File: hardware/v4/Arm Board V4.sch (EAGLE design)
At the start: 49 parts, among them IC2 REG1118, U1 SN74LS241DW, U2 XBEE-1B3, U3 LSM9DS0

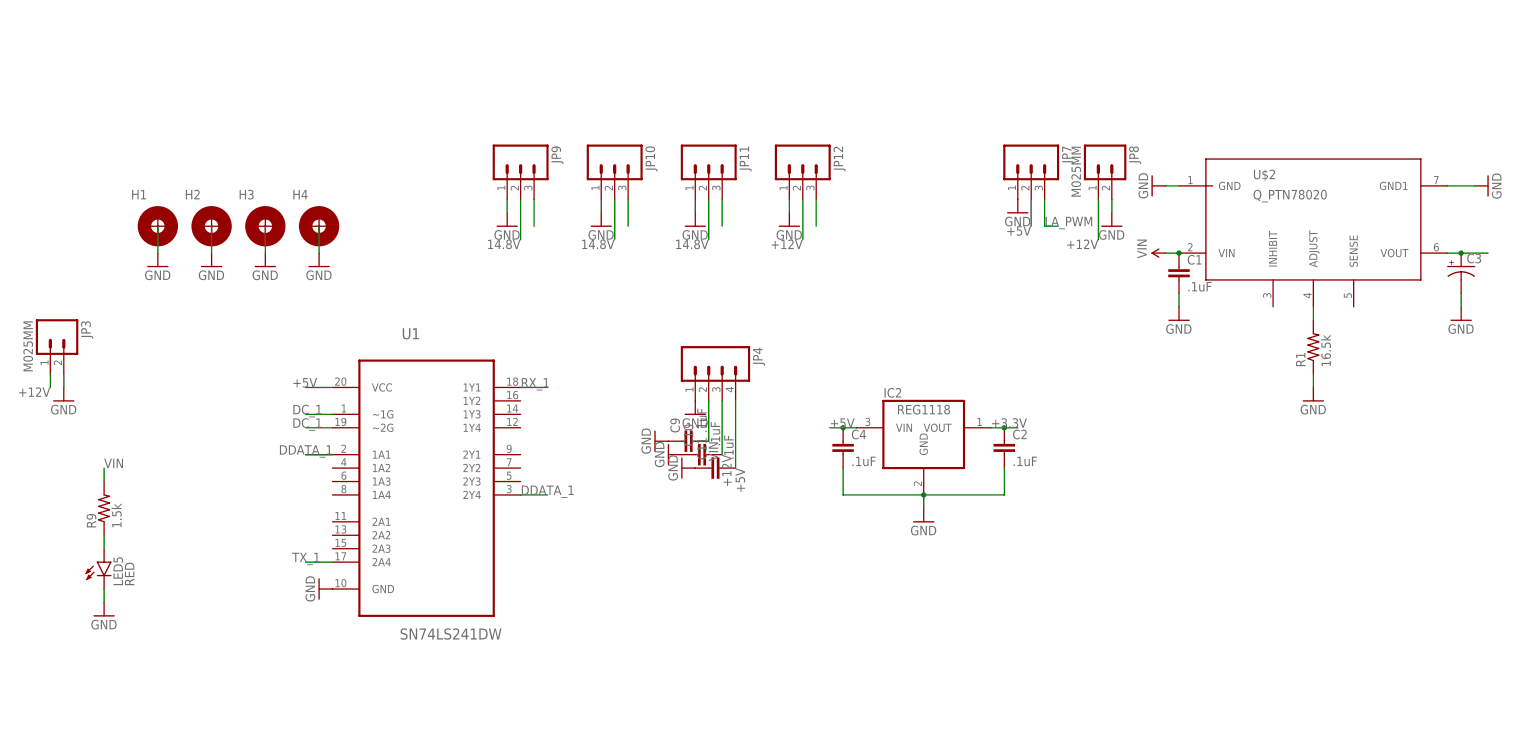
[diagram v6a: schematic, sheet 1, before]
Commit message: Just a few things with rearranging components
Moved some power connectors and a few pours
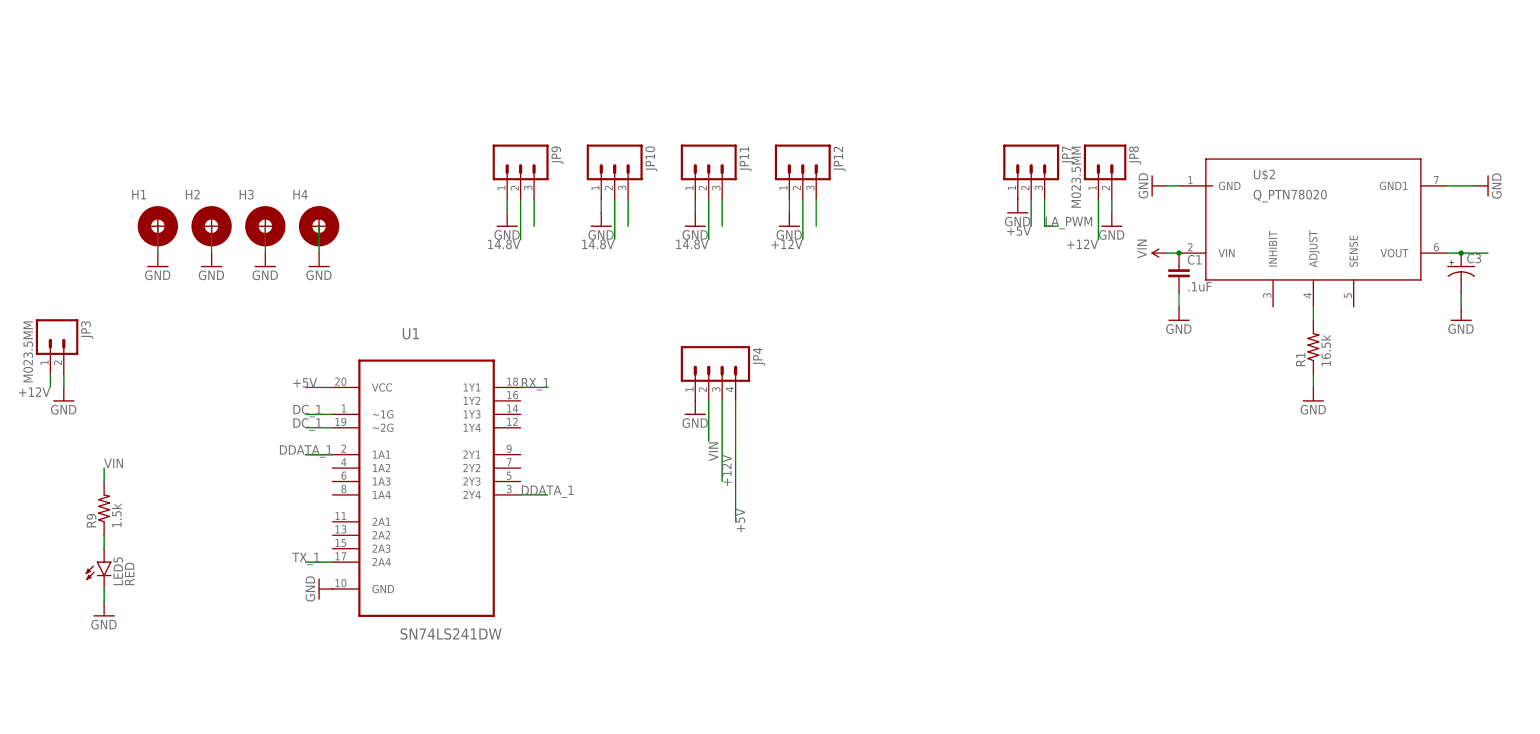
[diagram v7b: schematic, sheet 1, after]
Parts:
- removed C10, C11, C2, C4, C9: .1uF, SparkFun-Capacitors:CAP1206
- removed IC2: REG1118, burr-brown:REG1118
- JP3, JP8: value M025MM -> M023.5MM; device SparkFun-Connectors:M025MM -> SparkFun-Connectors:M023.5MM
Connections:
- removed net +3.3V: C2.1, IC2.VOUT, R12.2, R13.1, R14.1, U2.VDD
- net +12V: no longer C10.2
- net +3V3: now also R12.2, R13.1, R14.1, U2.VDD
- net +5V: no longer C11.2, C4.1, IC2.VIN
- net GND: no longer C10.1, C11.1, C2.2, C4.2, C9.1, IC2.GND
- net VIN: no longer C9.2
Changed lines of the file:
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@@
 <?xml version="1.0" encoding="utf-8"?>
 <!DOCTYPE eagle SYSTEM "eagle.dtd">
-<eagle version="6.5.0">
+<eagle version="7.1.0">
 <drawing>
 <settings>
@@
 <part name="U2" library="SparkFun" deviceset="XBEE-1" device="B3"/>
 <part name="JP7" library="SparkFun-Connectors" deviceset="M03" device="POLAR"/>
-<part name="JP8" library="SparkFun-Connectors" deviceset="M02" device="5MM"/>
+<part name="JP8" library="SparkFun-Connectors" deviceset="M02" device="3.5MM" value="M023.5MM"/>
 <part name="JP9" library="SparkFun-Connectors" deviceset="M03" device="POLAR"/>
 <part name="JP10" library="SparkFun-Connectors" deviceset="M03" device="POLAR"/>
@@
 <part name="C3" library="SparkFun-Passives" deviceset="CAP_POL" device="C"/>
 <part name="U$4" library="MAX3077" deviceset="MAX3077" device=""/>
-<part name="JP3" library="SparkFun-Connectors" deviceset="M02" device="5MM"/>
+<part name="JP3" library="SparkFun-Connectors" deviceset="M02" device="3.5MM" value="M023.5MM"/>
 <part name="GND6" library="SparkFun-Aesthetics" deviceset="GND" device=""/>
 <part name="U3" library="SparkFun-DigitalIC" deviceset="LSM9DS0" device=""/>
@@
 <part name="JP4" library="SparkFun-Connectors" deviceset="M04" device="SCREW"/>
 <part name="GND3" library="SparkFun-Aesthetics" deviceset="GND" device=""/>
-<part name="GND17" library="SparkFun-Aesthetics" deviceset="GND" device=""/>
-<part name="IC2" library="burr-brown" deviceset="REG1118" device=""/>
-<part name="C2" library="SparkFun-Capacitors" deviceset="CAP" device="1206" value=".1uF"/>
-<part name="C4" library="SparkFun-Capacitors" deviceset="CAP" device="1206" value=".1uF"/>
-<part name="C9" library="SparkFun-Capacitors" deviceset="CAP" device="1206" value=".1uF"/>
-<part name="C10" library="SparkFun-Capacitors" deviceset="CAP" device="1206" value=".1uF"/>
-<part name="C11" library="SparkFun-Capacitors" deviceset="CAP" device="1206" value=".1uF"/>
-<part name="GND22" library="SparkFun-Aesthetics" deviceset="GND" device=""/>
-<part name="GND24" library="SparkFun-Aesthetics" deviceset="GND" device=""/>
-<part name="GND29" library="SparkFun-Aesthetics" deviceset="GND" device=""/>
 </parts>
 <sheets>
@@
 <instance part="JP4" gate="G$1" x="129.54" y="10.16" rot="R270"/>
 <instance part="GND3" gate="1" x="127" y="2.54"/>
-<instance part="GND17" gate="1" x="170.18" y="-17.78"/>
-<instance part="IC2" gate="G$1" x="170.18" y="0"/>
-<instance part="C2" gate="G$1" x="185.42" y="-5.08"/>
-<instance part="C4" gate="G$1" x="154.94" y="-5.08"/>
-<instance part="C9" gate="G$1" x="127" y="-2.54" rot="R90"/>
-<instance part="C10" gate="G$1" x="129.54" y="-5.08" rot="R90"/>
-<instance part="C11" gate="G$1" x="132.08" y="-7.62" rot="R90"/>
-<instance part="GND22" gate="1" x="119.38" y="-2.54" rot="R270"/>
-<instance part="GND24" gate="1" x="121.92" y="-5.08" rot="R270"/>
-<instance part="GND29" gate="1" x="124.46" y="-7.62" rot="R270"/>
 </instances>
 <busses>
@@
 <pinref part="GND3" gate="1" pin="GND"/>
 </segment>
-<segment>
-<pinref part="IC2" gate="G$1" pin="GND"/>
-<pinref part="GND17" gate="1" pin="GND"/>
-<wire x1="170.18" y1="-15.24" x2="170.18" y2="-12.7" width="0.1524" layer="91"/>
-<pinref part="C4" gate="G$1" pin="2"/>
-<wire x1="154.94" y1="-7.62" x2="154.94" y2="-12.7" width="0.1524" layer="91"/>
-<wire x1="154.94" y1="-12.7" x2="170.18" y2="-12.7" width="0.1524" layer="91"/>
-<pinref part="C2" gate="G$1" pin="2"/>
-<wire x1="185.42" y1="-7.62" x2="185.42" y2="-12.7" width="0.1524" layer="91"/>
-<wire x1="185.42" y1="-12.7" x2="170.18" y2="-12.7" width="0.1524" layer="91"/>
-<junction x="170.18" y="-12.7"/>
-</segment>
-<segment>
-<pinref part="C9" gate="G$1" pin="1"/>
-<pinref part="GND22" gate="1" pin="GND"/>
-</segment>
-<segment>
-<pinref part="C10" gate="G$1" pin="1"/>
-<pinref part="GND24" gate="1" pin="GND"/>
-</segment>
-<segment>
-<pinref part="C11" gate="G$1" pin="1"/>
-<pinref part="GND29" gate="1" pin="GND"/>
-</segment>
 </net>
 <net name="+12V" class="0">
@@
 <segment>
 <pinref part="JP4" gate="G$1" pin="3"/>
-<wire x1="132.08" y1="5.08" x2="132.08" y2="-5.08" width="0.1524" layer="91"/>
+<wire x1="132.08" y1="5.08" x2="132.08" y2="-10.16" width="0.1524" layer="91"/>
 <label x="132.08" y="-5.08" size="1.778" layer="95" rot="R270"/>
-<pinref part="C10" gate="G$1" pin="2"/>
 </segment>
 </net>
@@
 <segment>
 <pinref part="JP4" gate="G$1" pin="4"/>
-<wire x1="134.62" y1="5.08" x2="134.62" y2="-7.62" width="0.1524" layer="91"/>
-<label x="134.62" y="-7.62" size="1.778" layer="95" rot="R270"/>
-<pinref part="C11" gate="G$1" pin="2"/>
-</segment>
-<segment>
-<wire x1="152.4" y1="0" x2="154.94" y2="0" width="0.1524" layer="91"/>
-<pinref part="IC2" gate="G$1" pin="VIN"/>
-<label x="152.4" y="0" size="1.778" layer="95"/>
-<pinref part="C4" gate="G$1" pin="1"/>
-<wire x1="154.94" y1="0" x2="157.48" y2="0" width="0.1524" layer="91"/>
-<junction x="154.94" y="0"/>
+<wire x1="134.62" y1="5.08" x2="134.62" y2="-17.78" width="0.1524" layer="91"/>
+<label x="134.62" y="-15.24" size="1.778" layer="95" rot="R270"/>
 </segment>
 </net>
@@
 <wire x1="129.54" y1="5.08" x2="129.54" y2="-2.54" width="0.1524" layer="91"/>
 <label x="129.54" y="-2.54" size="1.778" layer="95" rot="R270"/>
-<pinref part="C9" gate="G$1" pin="2"/>
 </segment>
 </net>
@@
 <pinref part="R9" gate="G$1" pin="1"/>
 <pinref part="LED5" gate="G$1" pin="A"/>
-</segment>
-</net>
-<net name="+3.3V" class="0">
-<segment>
-<wire x1="182.88" y1="0" x2="185.42" y2="0" width="0.1524" layer="91"/>
-<pinref part="IC2" gate="G$1" pin="VOUT"/>
-<label x="182.88" y="0" size="1.778" layer="95"/>
-<pinref part="C2" gate="G$1" pin="1"/>
-<wire x1="185.42" y1="0" x2="187.96" y2="0" width="0.1524" layer="91"/>
-<junction x="185.42" y="0"/>
 </segment>
 </net>
@@
 </segment>
 </net>
-<net name="+3.3V" class="0">
+<net name="+3V3" class="0">
 <segment>
 <wire x1="27.94" y1="25.4" x2="2.54" y2="25.4" width="0.1524" layer="91"/>

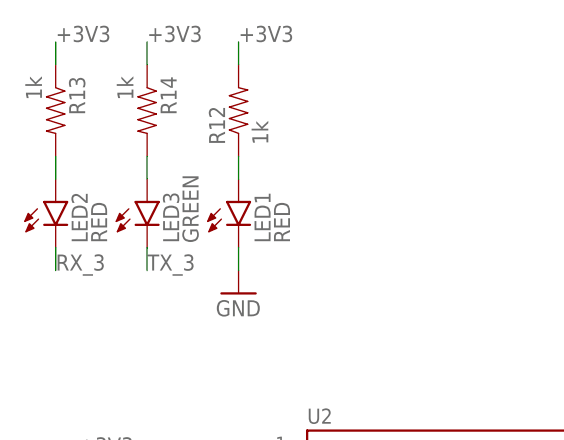
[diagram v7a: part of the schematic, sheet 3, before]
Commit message: Seeing how small it can go
It does not really work well but can be evaluated
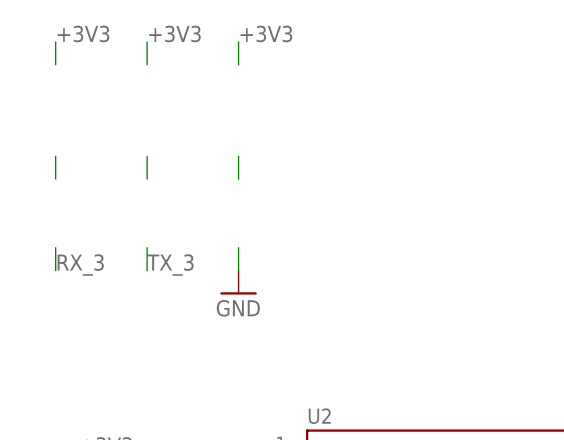
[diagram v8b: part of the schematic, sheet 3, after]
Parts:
- removed H1, H2, H3, H4: (no value), Lib_TH:H_MNTHOLE_#4
- removed LED1, LED2: RED, SparkFun-LED:LED-RED0603
- removed LED3: GREEN, SparkFun-LED:LED-GREEN0603
- removed R12, R13, R14: 1k, SparkFun-Passives:RESISTOR1206
- added S1, S2, S3, S4: STANDOFF_ELECTRICAL, SparkFun-Electromechanical:STANDOFF_ELECTRICAL
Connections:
- removed net N$38: LED1.A, R12.1
- removed net N$4: LED2.A, R13.2
- removed net N$6: LED3.A, R14.2
- net +3V3: no longer R12.2, R13.1, R14.1
- net GND: no longer H1.1, H2.1, H3.1, H4.1, LED1.C
- net RX_3: no longer LED2.C
- net TX_3: no longer LED3.C
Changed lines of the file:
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@@
 <part name="R11" library="SparkFun-Passives" deviceset="RESISTOR" device="1206" value="120 Ohm"/>
 <part name="C12" library="SparkFun-Capacitors" deviceset="CAP" device="1206" value=".1uF"/>
-<part name="H1" library="Lib_TH" deviceset="H_MNTHOLE" device="_#4"/>
-<part name="H2" library="Lib_TH" deviceset="H_MNTHOLE" device="_#4"/>
-<part name="H3" library="Lib_TH" deviceset="H_MNTHOLE" device="_#4"/>
-<part name="H4" library="Lib_TH" deviceset="H_MNTHOLE" device="_#4"/>
-<part name="GND11" library="SparkFun-Aesthetics" deviceset="GND" device=""/>
-<part name="GND12" library="SparkFun-Aesthetics" deviceset="GND" device=""/>
-<part name="GND13" library="SparkFun-Aesthetics" deviceset="GND" device=""/>
-<part name="GND14" library="SparkFun-Aesthetics" deviceset="GND" device=""/>
-<part name="R12" library="SparkFun-Passives" deviceset="RESISTOR" device="1206" value="1k"/>
-<part name="LED1" library="SparkFun-LED" deviceset="LED-RED" device="0603" value="RED"/>
 <part name="GND28" library="SparkFun" deviceset="GND" device=""/>
-<part name="LED2" library="SparkFun-LED" deviceset="LED-RED" device="0603" value="RED"/>
-<part name="LED3" library="SparkFun-LED" deviceset="LED-GREEN" device="0603" value="GREEN"/>
-<part name="R13" library="SparkFun-Passives" deviceset="RESISTOR" device="1206" value="1k"/>
-<part name="R14" library="SparkFun-Passives" deviceset="RESISTOR" device="1206" value="1k"/>
 <part name="U2" library="SparkFun" deviceset="XBEE-1" device="B3"/>
 <part name="JP7" library="SparkFun-Connectors" deviceset="M03" device="POLAR"/>
@@
 <part name="JP4" library="SparkFun-Connectors" deviceset="M04" device="SCREW"/>
 <part name="GND3" library="SparkFun-Aesthetics" deviceset="GND" device=""/>
+<part name="S1" library="SparkFun-Electromechanical" deviceset="STANDOFF_ELECTRICAL" device=""/>
+<part name="S2" library="SparkFun-Electromechanical" deviceset="STANDOFF_ELECTRICAL" device=""/>
+<part name="S3" library="SparkFun-Electromechanical" deviceset="STANDOFF_ELECTRICAL" device=""/>
+<part name="S4" library="SparkFun-Electromechanical" deviceset="STANDOFF_ELECTRICAL" device=""/>
 </parts>
 <sheets>
@@
 </plain>
 <instances>
-<instance part="H1" gate="G$1" x="25.4" y="38.1"/>
-<instance part="H2" gate="G$1" x="35.56" y="38.1"/>
-<instance part="H3" gate="G$1" x="45.72" y="38.1"/>
-<instance part="H4" gate="G$1" x="55.88" y="38.1"/>
-<instance part="GND11" gate="1" x="25.4" y="30.48"/>
-<instance part="GND12" gate="1" x="35.56" y="30.48"/>
-<instance part="GND13" gate="1" x="45.72" y="30.48"/>
-<instance part="GND14" gate="1" x="55.88" y="30.48"/>
 <instance part="JP7" gate="G$1" x="190.5" y="50.8" rot="R270"/>
 <instance part="JP8" gate="G$1" x="203.2" y="50.8" rot="R270"/>
@@
 <instance part="JP4" gate="G$1" x="129.54" y="10.16" rot="R270"/>
 <instance part="GND3" gate="1" x="127" y="2.54"/>
+<instance part="S1" gate="G$1" x="43.18" y="73.66" rot="R270"/>
+<instance part="S2" gate="G$1" x="55.88" y="73.66" rot="R270"/>
+<instance part="S3" gate="G$1" x="68.58" y="73.66" rot="R270"/>
+<instance part="S4" gate="G$1" x="81.28" y="73.66" rot="R270"/>
 </instances>
 <busses>
@@
 <nets>
 <net name="GND" class="0">
-<segment>
-<pinref part="H1" gate="G$1" pin="1"/>
-<pinref part="GND11" gate="1" pin="GND"/>
-<wire x1="25.4" y1="33.02" x2="25.4" y2="38.1" width="0.1524" layer="91"/>
-</segment>
-<segment>
-<pinref part="H2" gate="G$1" pin="1"/>
-<pinref part="GND12" gate="1" pin="GND"/>
-<wire x1="35.56" y1="33.02" x2="35.56" y2="38.1" width="0.1524" layer="91"/>
-</segment>
-<segment>
-<pinref part="H3" gate="G$1" pin="1"/>
-<pinref part="GND13" gate="1" pin="GND"/>
-<wire x1="45.72" y1="33.02" x2="45.72" y2="38.1" width="0.1524" layer="91"/>
-</segment>
-<segment>
-<pinref part="H4" gate="G$1" pin="1"/>
-<pinref part="GND14" gate="1" pin="GND"/>
-<wire x1="55.88" y1="33.02" x2="55.88" y2="38.1" width="0.1524" layer="91"/>
-</segment>
 <segment>
 <pinref part="JP9" gate="G$1" pin="1"/>
@@
 </plain>
 <instances>
-<instance part="R12" gate="G$1" x="25.4" y="63.5" rot="R90"/>
-<instance part="LED1" gate="G$1" x="25.4" y="53.34"/>
 <instance part="GND28" gate="1" x="25.4" y="43.18"/>
-<instance part="LED2" gate="G$1" x="5.08" y="53.34"/>
-<instance part="LED3" gate="G$1" x="15.24" y="53.34"/>
-<instance part="R13" gate="G$1" x="5.08" y="63.5" rot="R270"/>
-<instance part="R14" gate="G$1" x="15.24" y="63.5" rot="R270"/>
 <instance part="U2" gate="G$1" x="48.26" y="15.24"/>
 </instances>
@@
 <segment>
 <wire x1="25.4" y1="48.26" x2="25.4" y2="45.72" width="0.1524" layer="91"/>
-<pinref part="LED1" gate="G$1" pin="C"/>
 <pinref part="GND28" gate="1" pin="GND"/>
 </segment>
@@
 <segment>
 <wire x1="25.4" y1="55.88" x2="25.4" y2="58.42" width="0.1524" layer="91"/>
-<pinref part="R12" gate="G$1" pin="1"/>
-<pinref part="LED1" gate="G$1" pin="A"/>
 </segment>
 </net>
@@
 <segment>
 <wire x1="5.08" y1="58.42" x2="5.08" y2="55.88" width="0.1524" layer="91"/>
-<pinref part="LED2" gate="G$1" pin="A"/>
-<pinref part="R13" gate="G$1" pin="2"/>
 </segment>
 </net>
@@
 <segment>
 <wire x1="15.24" y1="58.42" x2="15.24" y2="55.88" width="0.1524" layer="91"/>
-<pinref part="LED3" gate="G$1" pin="A"/>
-<pinref part="R14" gate="G$1" pin="2"/>
 </segment>
 </net>
@@
 <segment>
 <wire x1="5.08" y1="68.58" x2="5.08" y2="71.12" width="0.1524" layer="91"/>
-<pinref part="R13" gate="G$1" pin="1"/>
 <label x="5.08" y="71.12" size="1.778" layer="95"/>
 </segment>
 <segment>
 <wire x1="25.4" y1="71.12" x2="25.4" y2="68.58" width="0.1524" layer="91"/>
-<pinref part="R12" gate="G$1" pin="2"/>
 <label x="25.4" y="71.12" size="1.778" layer="95"/>
 </segment>
 <segment>
 <wire x1="15.24" y1="68.58" x2="15.24" y2="71.12" width="0.1524" layer="91"/>
-<pinref part="R14" gate="G$1" pin="1"/>
 <label x="15.24" y="71.12" size="1.778" layer="95"/>
 </segment>
@@
 <segment>
 <wire x1="5.08" y1="48.26" x2="5.08" y2="45.72" width="0.1524" layer="91"/>
-<pinref part="LED2" gate="G$1" pin="C"/>
 <label x="5.08" y="45.72" size="1.778" layer="95"/>
 </segment>
@@
 <segment>
 <wire x1="15.24" y1="48.26" x2="15.24" y2="45.72" width="0.1524" layer="91"/>
-<pinref part="LED3" gate="G$1" pin="C"/>
 <label x="15.24" y="45.72" size="1.778" layer="95"/>
 </segment>
